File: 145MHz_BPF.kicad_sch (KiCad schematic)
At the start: 4 parts, among them J1 Conn_01x02_Socket, J2 Conn_01x02_Socket, J3 Conn_01x01_Socket, U1 SXBP-140

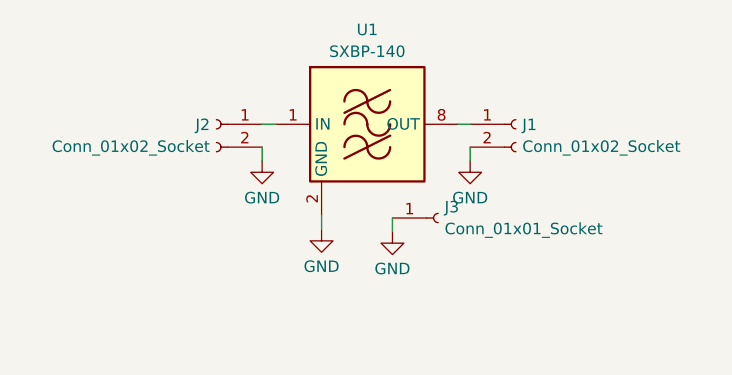
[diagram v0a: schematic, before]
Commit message: mmcx connector footprint added
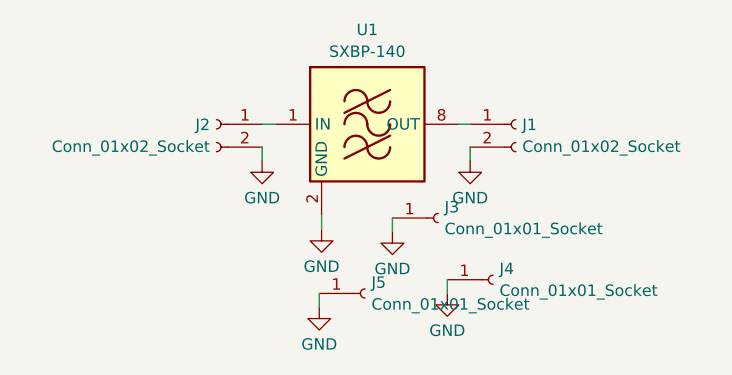
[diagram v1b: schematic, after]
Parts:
- added J4, J5: Conn_01x01_Socket, SolderWire-0.1sqmm_1x01_D0.4mm_OD1mm, symbol Connector:Conn_01x01_Socket
- J1, J2: footprint Connector_Wire:SolderWire-0.1sqmm_1x02_P3.6mm_D0.4mm_OD1mm -> Connector_Coaxial:MMCX_Molex_73415-1471_Vertical
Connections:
- net GND: now also J4.1 (Pin_1), J5.1 (Pin_1)
